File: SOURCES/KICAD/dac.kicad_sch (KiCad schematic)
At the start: 172 parts

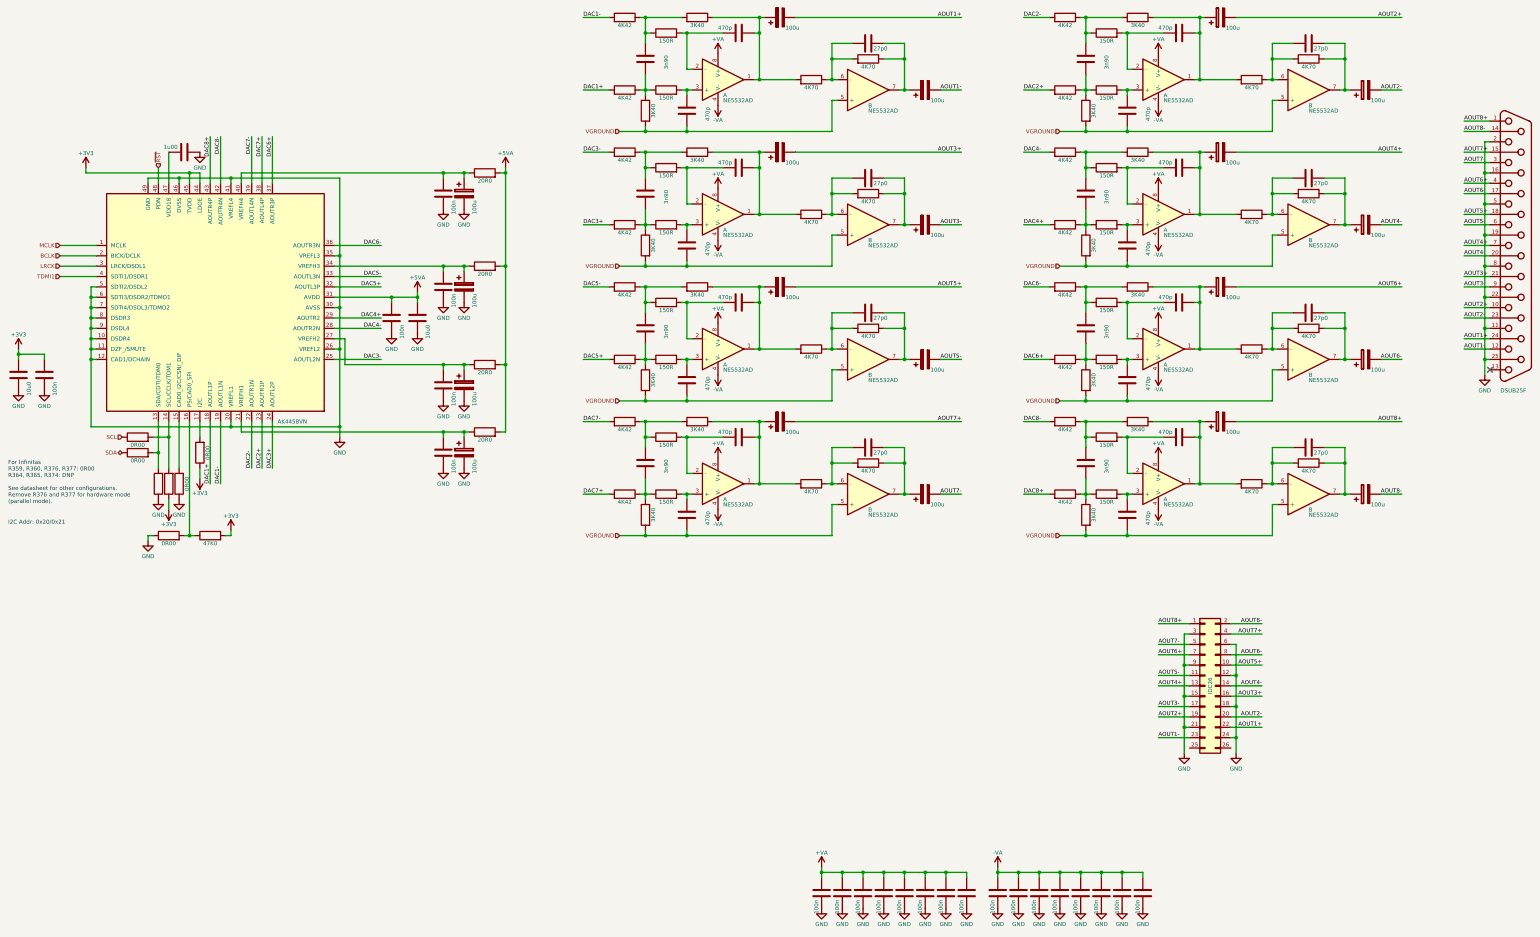
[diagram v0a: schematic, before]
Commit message: Rescue footprints to local library
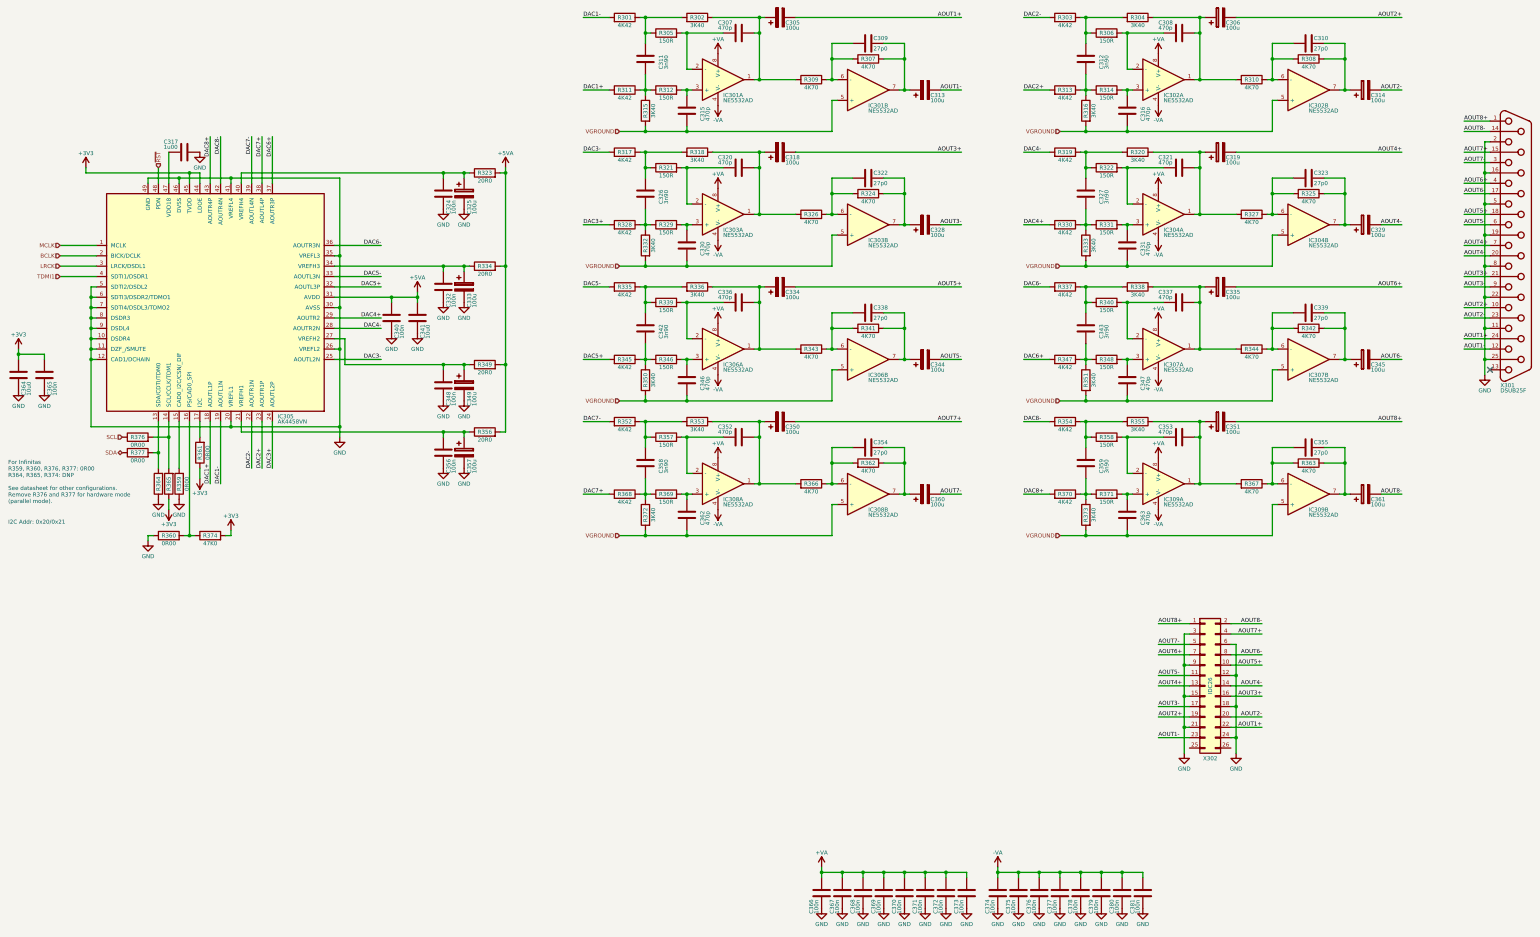
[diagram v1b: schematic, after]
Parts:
- C305, C306, C313, C314, C318, C319, C325, C328, C329, C333, C334, C335, C344, C345, C349, C350, C351, C357, C360, C361: renamed from ?; footprint Capacitors_ThroughHole:C_Radial_D5_L11_P2 -> AnalogIO-x8:RD2_D5_L11
- C307, C308, C309, C310, C311, C312, C315, C316, C317, C320, C321, C322, C323, C324, C326, C327, C330, C331, C332, C336, C337, C338, C339, C340, C341, C342, C343, C346, C347, C348, C352, C353, C354, C355, C356, C358, C359, C362, C363, C364, C365, C366, C367, C368, C369, C370, C371, C372, C373, C374, C375, C376, C377, C378, C379, C380, C381: renamed from ?; footprint rklib:C0805-X7R -> AnalogIO-x8:C0805-X7R
- X301: renamed from ?; footprint rklib:DSUB25FC -> AnalogIO-x8:DSUB25FC
- X302: renamed from ?; footprint Connect:IDC_Header_Straight_26pins -> AnalogIO-x8:IDC26
- gave numbers to parts that had none: 85
